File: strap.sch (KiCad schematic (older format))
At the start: 20 parts, among them SW1 SW_DIP_x08, U3 74LVC1G06, U4 74LVC1G06, U5 PCA9306, U8 24AA0x

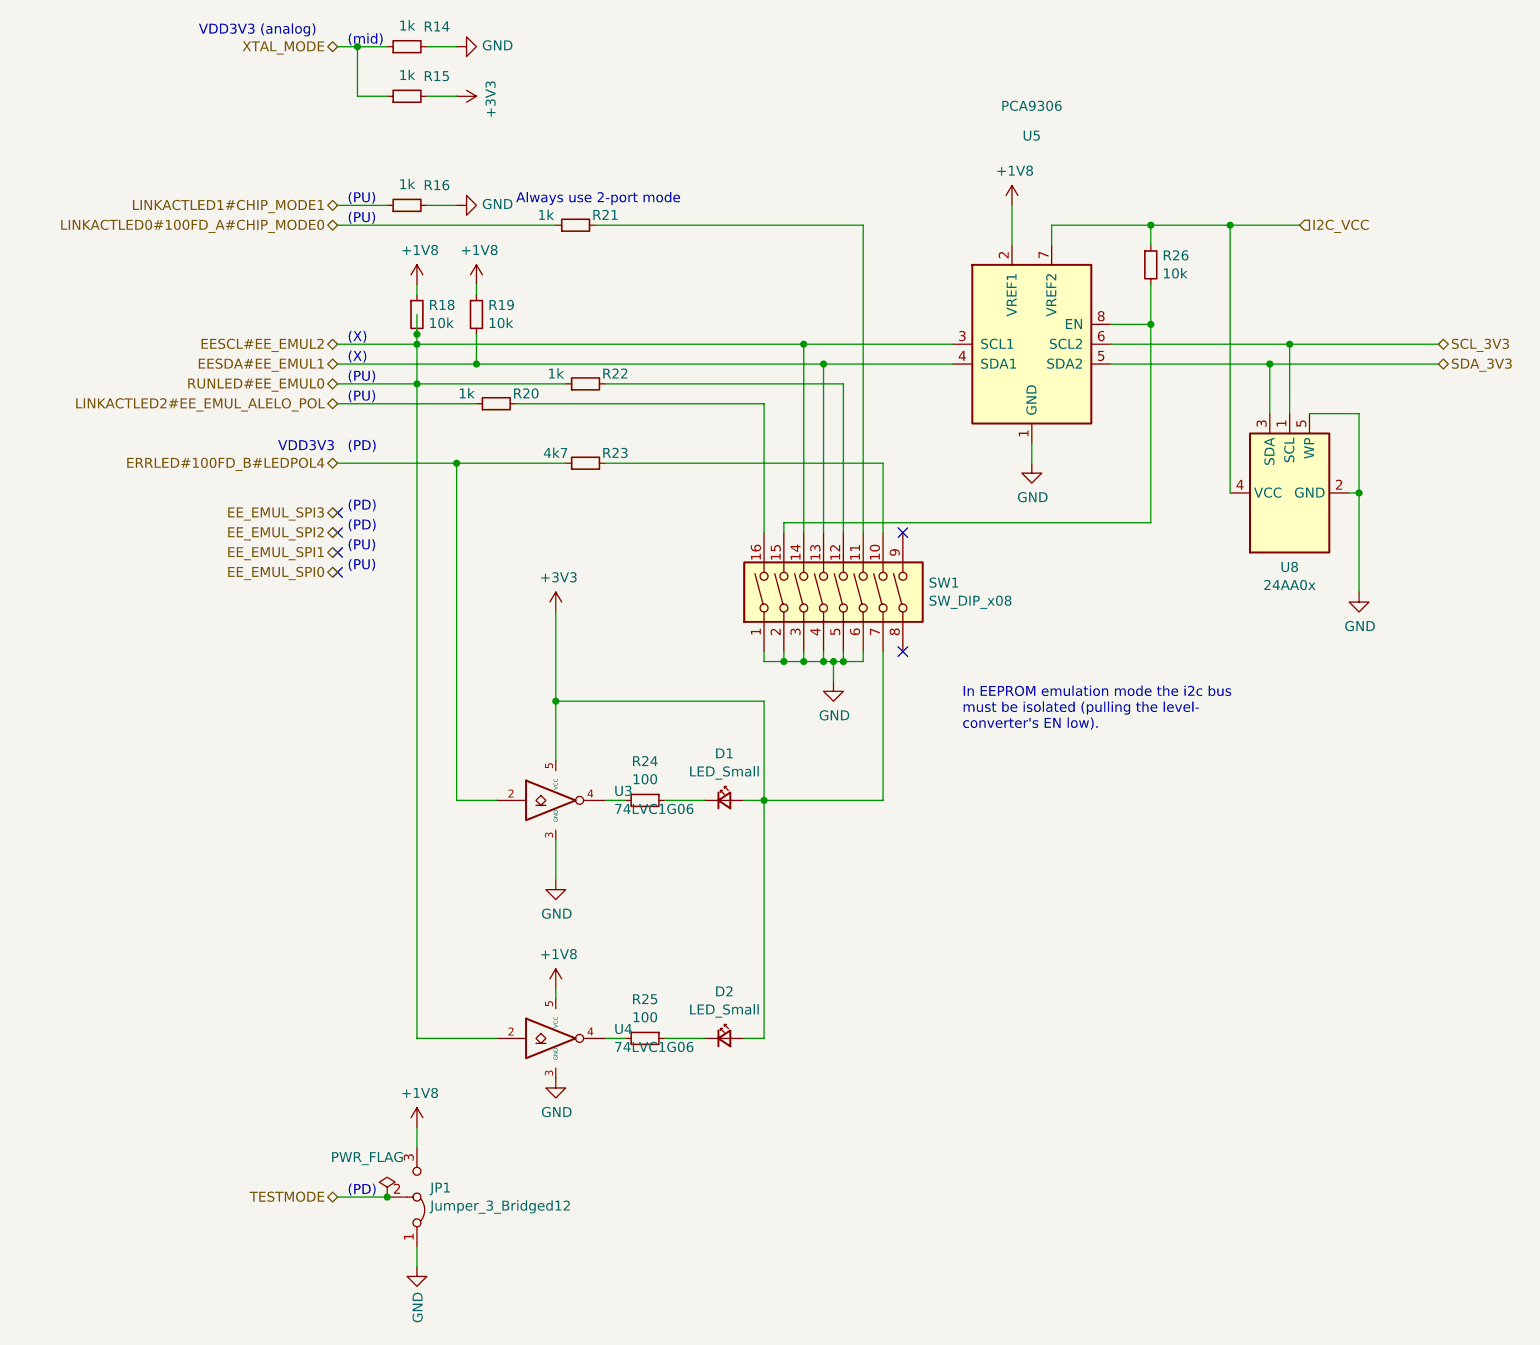
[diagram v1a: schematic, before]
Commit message: reannotated for merging with te0715 development board
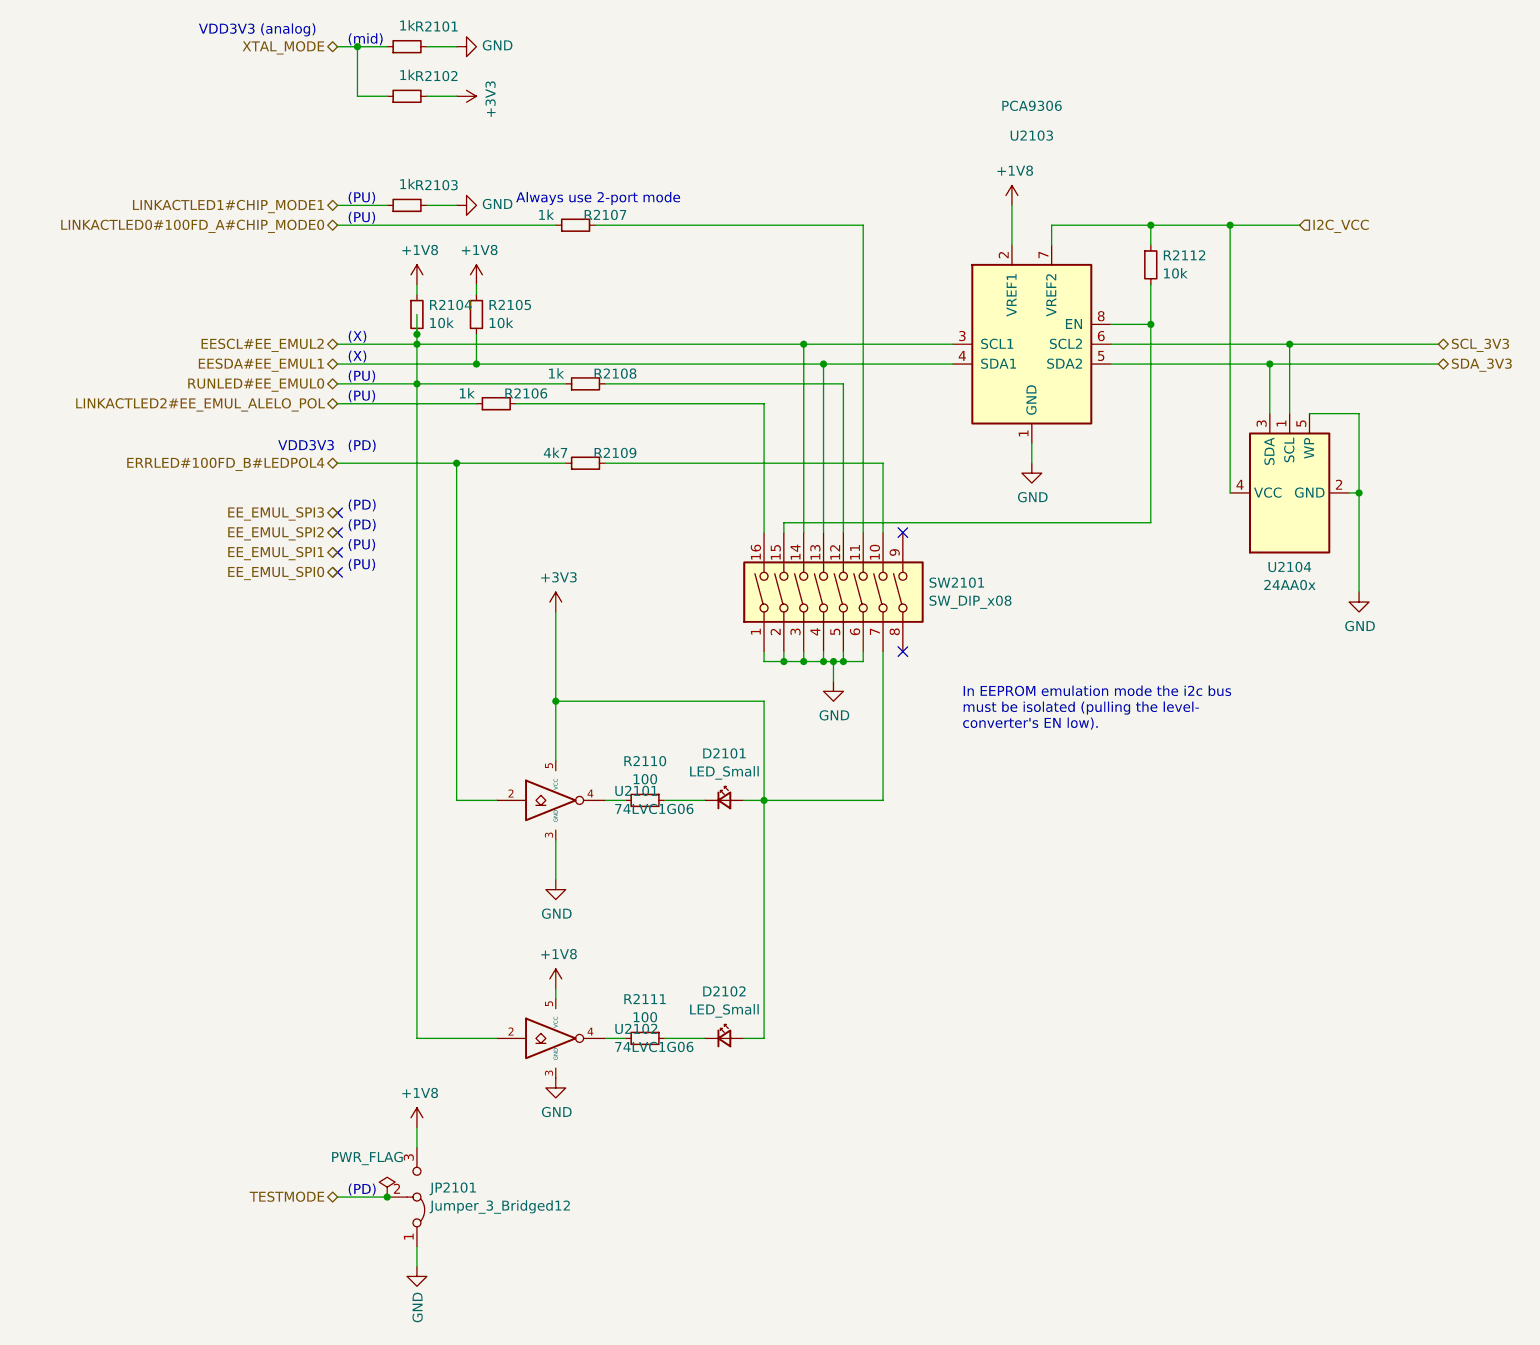
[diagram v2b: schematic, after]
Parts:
- renumbered D1 to D2101, D2 to D2102, JP1 to JP2101, SW1 to SW2101, U3 to U2101, U4 to U2102, U5 to U2103, U8 to U2104
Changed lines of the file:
@@
 AR Path="/60DC28BD/60E60393" Ref="R?"  Part="1"
 AR Path="/60E5E32B/60E60393" Ref="R16"  Part="1"
-AR Path="/60DB2574/60E5E32B/60E60393" Ref="R16"  Part="1"
-F 0 "R16" V 4250 1950 50  0000 C CNN
+AR Path="/60DB2574/60E5E32B/60E60393" Ref="R2103"  Part="1"
+F 0 "R2103" V 4250 1950 50  0000 C CNN
 F 1 "1k" V 4255 2100 50  0000 C CNN
 F 2 "Resistor_SMD:R_0603_1608Metric" H 4150 2100 50  0001 C CNN
@@
 AR Path="/60DC28BD/60E79F58" Ref="R?"  Part="1"
 AR Path="/60E5E32B/60E79F58" Ref="R18"  Part="1"
-AR Path="/60DB2574/60E5E32B/60E79F58" Ref="R18"  Part="1"
-F 0 "R18" H 4259 2696 50  0000 L CNN
+AR Path="/60DB2574/60E5E32B/60E79F58" Ref="R2104"  Part="1"
+F 0 "R2104" H 4259 2696 50  0000 L CNN
 F 1 "10k" H 4259 2605 50  0000 L CNN
 F 2 "Resistor_SMD:R_0603_1608Metric" H 4200 2650 50  0001 C CNN
@@
 AR Path="/60DC28BD/60E7C06A" Ref="R?"  Part="1"
 AR Path="/60E5E32B/60E7C06A" Ref="R19"  Part="1"
-AR Path="/60DB2574/60E5E32B/60E7C06A" Ref="R19"  Part="1"
-F 0 "R19" H 4559 2696 50  0000 L CNN
+AR Path="/60DB2574/60E5E32B/60E7C06A" Ref="R2105"  Part="1"
+F 0 "R2105" H 4559 2696 50  0000 L CNN
 F 1 "10k" H 4559 2605 50  0000 L CNN
 F 2 "Resistor_SMD:R_0603_1608Metric" H 4500 2650 50  0001 C CNN
@@
 AR Path="/60DC28BD/60E7CBCF" Ref="R?"  Part="1"
 AR Path="/60E5E32B/60E7CBCF" Ref="R14"  Part="1"
-AR Path="/60DB2574/60E5E32B/60E7CBCF" Ref="R14"  Part="1"
-F 0 "R14" V 4250 1150 50  0000 C CNN
+AR Path="/60DB2574/60E5E32B/60E7CBCF" Ref="R2101"  Part="1"
+F 0 "R2101" V 4250 1150 50  0000 C CNN
 F 1 "1k" V 4255 1300 50  0000 C CNN
 F 2 "Resistor_SMD:R_0603_1608Metric" H 4150 1300 50  0001 C CNN
@@
 AR Path="/60DC28BD/60E86BE2" Ref="R?"  Part="1"
 AR Path="/60E5E32B/60E86BE2" Ref="R22"  Part="1"
-AR Path="/60DB2574/60E5E32B/60E86BE2" Ref="R22"  Part="1"
-F 0 "R22" V 5100 2850 50  0000 C CNN
+AR Path="/60DB2574/60E5E32B/60E86BE2" Ref="R2108"  Part="1"
+F 0 "R2108" V 5100 2850 50  0000 C CNN
 F 1 "1k" V 5100 3150 50  0000 C CNN
 F 2 "Resistor_SMD:R_0603_1608Metric" H 5050 3000 50  0001 C CNN
@@
 AR Path="/60DC28BD/60E8A4A5" Ref="R?"  Part="1"
 AR Path="/60E5E32B/60E8A4A5" Ref="R20"  Part="1"
-AR Path="/60DB2574/60E5E32B/60E8A4A5" Ref="R20"  Part="1"
-F 0 "R20" V 4650 2950 50  0000 C CNN
+AR Path="/60DB2574/60E5E32B/60E8A4A5" Ref="R2106"  Part="1"
+F 0 "R2106" V 4650 2950 50  0000 C CNN
 F 1 "1k" V 4650 3250 50  0000 C CNN
 F 2 "Resistor_SMD:R_0603_1608Metric" H 4600 3100 50  0001 C CNN
@@
 AR Path="/60DC28BD/60E8A76F" Ref="R?"  Part="1"
 AR Path="/60E5E32B/60E8A76F" Ref="R23"  Part="1"
-AR Path="/60DB2574/60E5E32B/60E8A76F" Ref="R23"  Part="1"
-F 0 "R23" V 5100 3250 50  0000 C CNN
+AR Path="/60DB2574/60E5E32B/60E8A76F" Ref="R2109"  Part="1"
+F 0 "R2109" V 5100 3250 50  0000 C CNN
 F 1 "4k7" V 5100 3550 50  0000 C CNN
 F 2 "Resistor_SMD:R_0603_1608Metric" H 5050 3400 50  0001 C CNN
@@
 AR Path="/60DC28BD/60E8AAF4" Ref="R?"  Part="1"
 AR Path="/60E5E32B/60E8AAF4" Ref="R21"  Part="1"
-AR Path="/60DB2574/60E5E32B/60E8AAF4" Ref="R21"  Part="1"
-F 0 "R21" V 5050 2050 50  0000 C CNN
+AR Path="/60DB2574/60E5E32B/60E8AAF4" Ref="R2107"  Part="1"
+F 0 "R2107" V 5050 2050 50  0000 C CNN
 F 1 "1k" V 5050 2350 50  0000 C CNN
 F 2 "Resistor_SMD:R_0603_1608Metric" H 5000 2200 50  0001 C CNN
@@
 	5100 2200 6450 2200
 $Comp
-L Interface:PCA9306 U5
+L Interface:PCA9306 U2103
 U 1 1 60E8C646
 P 7300 2800
-F 0 "U5" H 7300 3850 50  0000 C CNN
+F 0 "U2103" H 7300 3850 50  0000 C CNN
 F 1 "PCA9306" H 7300 4000 50  0000 C CNN
 F 2 "Package_SO:TSSOP-8_3x3mm_P0.65mm" H 6900 3150 50  0001 C CNN
@@
 AR Path="/60DC28BD/60E9E985" Ref="R?"  Part="1"
 AR Path="/60E5E32B/60E9E985" Ref="R24"  Part="1"
-AR Path="/60DB2574/60E5E32B/60E9E985" Ref="R24"  Part="1"
-F 0 "R24" V 5154 5100 50  0000 C CNN
+AR Path="/60DB2574/60E5E32B/60E9E985" Ref="R2110"  Part="1"
+F 0 "R2110" V 5154 5100 50  0000 C CNN
 F 1 "100" V 5245 5100 50  0000 C CNN
 F 2 "Resistor_SMD:R_0603_1608Metric" H 5350 5100 50  0001 C CNN
@@
 	5150 5100 5250 5100
 $Comp
-L Device:LED_Small D1
+L Device:LED_Small D2101
 U 1 1 60EA2110
 P 5750 5100
-F 0 "D1" H 5750 5335 50  0000 C CNN
+F 0 "D2101" H 5750 5335 50  0000 C CNN
 F 1 "LED_Small" H 5750 5244 50  0000 C CNN
 F 2 "LED_SMD:LED_0603_1608Metric" V 5750 5100 50  0001 C CNN
@@
 AR Path="/60DC28BD/60EA51EB" Ref="R?"  Part="1"
 AR Path="/60E5E32B/60EA51EB" Ref="R25"  Part="1"
-AR Path="/60DB2574/60E5E32B/60EA51EB" Ref="R25"  Part="1"
-F 0 "R25" V 5154 6300 50  0000 C CNN
+AR Path="/60DB2574/60E5E32B/60EA51EB" Ref="R2111"  Part="1"
+F 0 "R2111" V 5154 6300 50  0000 C CNN
 F 1 "100" V 5245 6300 50  0000 C CNN
 F 2 "Resistor_SMD:R_0603_1608Metric" H 5350 6300 50  0001 C CNN
@@
 	5150 6300 5250 6300
 $Comp
-L Device:LED_Small D2
+L Device:LED_Small D2102
 U 1 1 60EA51F6
 P 5750 6300
-F 0 "D2" H 5750 6535 50  0000 C CNN
+F 0 "D2102" H 5750 6535 50  0000 C CNN
 F 1 "LED_Small" H 5750 6444 50  0000 C CNN
 F 2 "LED_SMD:LED_0603_1608Metric" V 5750 6300 50  0001 C CNN
@@
 AR Path="/60DC28BD/60EACF8C" Ref="R?"  Part="1"
 AR Path="/60E5E32B/60EACF8C" Ref="R26"  Part="1"
-AR Path="/60DB2574/60E5E32B/60EACF8C" Ref="R26"  Part="1"
-F 0 "R26" H 7959 2446 50  0000 L CNN
+AR Path="/60DB2574/60E5E32B/60EACF8C" Ref="R2112"  Part="1"
+F 0 "R2112" H 7959 2446 50  0000 L CNN
 F 1 "10k" H 7959 2355 50  0000 L CNN
 F 2 "Resistor_SMD:R_0603_1608Metric" H 7900 2400 50  0001 C CNN
@@
 AR Path="/60DC28BD/60DB9030" Ref="R?"  Part="1"
 AR Path="/60E5E32B/60DB9030" Ref="R15"  Part="1"
-AR Path="/60DB2574/60E5E32B/60DB9030" Ref="R15"  Part="1"
-F 0 "R15" V 4250 1400 50  0000 C CNN
+AR Path="/60DB2574/60E5E32B/60DB9030" Ref="R2102"  Part="1"
+F 0 "R2102" V 4250 1400 50  0000 C CNN
 F 1 "1k" V 4255 1550 50  0000 C CNN
 F 2 "Resistor_SMD:R_0603_1608Metric" H 4150 1550 50  0001 C CNN
@@
 Connection ~ 7900 2200
 $Comp
-L fmc:74LVC1G06 U3
+L fmc:74LVC1G06 U2101
 U 1 1 611336A3
 P 4900 5100
-F 0 "U3" H 5194 5146 50  0000 L CNN
+F 0 "U2101" H 5194 5146 50  0000 L CNN
 F 1 "74LVC1G06" H 5194 5055 50  0000 L CNN
 F 2 "Package_TO_SOT_SMD:SOT-553" H 4900 5100 50  0001 C CNN
@@
 	4900 4900 4900 4600
 $Comp
-L fmc:74LVC1G06 U4
+L fmc:74LVC1G06 U2102
 U 1 1 611387E0
 P 4900 6300
-F 0 "U4" H 5194 6346 50  0000 L CNN
+F 0 "U2102" H 5194 6346 50  0000 L CNN
 F 1 "74LVC1G06" H 5194 6255 50  0000 L CNN
 F 2 "Package_TO_SOT_SMD:SOT-553" H 4900 6300 50  0001 C CNN
@@
 	4900 6050 4900 6100
 $Comp
-L fmc:24AA0x U8
+L fmc:24AA0x U2104
 U 1 1 611D5C36
 P 8600 3550
-F 0 "U8" V 8225 3550 50  0000 C CNN
+F 0 "U2104" V 8225 3550 50  0000 C CNN
 F 1 "24AA0x" V 8134 3550 50  0000 C CNN
 F 2 "Package_TO_SOT_SMD:SOT-23-5" H 8600 3550 50  0001 C CNN
@@
 Connection ~ 8500 2900
 $Comp
-L Switch:SW_DIP_x08 SW1
+L Switch:SW_DIP_x08 SW2101
 U 1 1 60E7D790
 P 6350 4050
-F 0 "SW1" V 6396 3620 50  0000 R CNN
+F 0 "SW2101" V 6396 3620 50  0000 R CNN
 F 1 "SW_DIP_x08" V 6305 3620 50  0000 R CNN
 F 2 "Button_Switch_SMD:SW_DIP_SPSTx08_Slide_Copal_CHS-08A_W5.08mm_P1.27mm_JPin" H 6350 4050 50  0001 C CNN
@@
 NoConn ~ 6650 3750
 $Comp
-L Jumper:Jumper_3_Bridged12 JP1
+L Jumper:Jumper_3_Bridged12 JP2101
 U 1 1 60E8D294
 P 4200 7100
-F 0 "JP1" V 4246 7167 50  0000 L CNN
+F 0 "JP2101" V 4246 7167 50  0000 L CNN
 F 1 "Jumper_3_Bridged12" V 4155 7167 50  0000 L CNN
 F 2 "Connector_PinHeader_1.27mm:PinHeader_1x03_P1.27mm_Vertical" H 4200 7100 50  0001 C CNN
